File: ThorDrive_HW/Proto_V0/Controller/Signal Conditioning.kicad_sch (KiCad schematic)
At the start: 13 parts, among them U2 LM324, U3 LM324

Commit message: update
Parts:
- C3, C4, C5, C6: footprint (none) -> Capacitor_SMD:C_0805_2012Metric_Pad1.18x1.45mm_HandSolder
- R3, R4, R5: footprint (none) -> Resistor_SMD:R_1206_3216Metric_Pad1.30x1.75mm_HandSolder
- R6, R7, R8, R9: footprint (none) -> Resistor_SMD:R_0805_2012Metric_Pad1.20x1.40mm_HandSolder
- U2, U3: footprint (none) -> Package_SO:SOIC-14_3.9x8.7mm_P1.27mm
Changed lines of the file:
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@@
 			)
 		)
-		(property "Footprint" ""
+		(property "Footprint" "Package_SO:SOIC-14_3.9x8.7mm_P1.27mm"
 			(at 57.15 86.36 0)
 			(effects
@@
 			)
 		)
-		(property "Footprint" ""
+		(property "Footprint" "Resistor_SMD:R_1206_3216Metric_Pad1.30x1.75mm_HandSolder"
 			(at 47.752 127 90)
 			(effects
@@
 			)
 		)
-		(property "Footprint" ""
+		(property "Footprint" "Package_SO:SOIC-14_3.9x8.7mm_P1.27mm"
 			(at 175.26 80.01 0)
 			(effects
@@
 			)
 		)
-		(property "Footprint" ""
+		(property "Footprint" "Package_SO:SOIC-14_3.9x8.7mm_P1.27mm"
 			(at 55.88 45.72 0)
 			(effects
@@
 			)
 		)
-		(property "Footprint" ""
+		(property "Footprint" "Resistor_SMD:R_0805_2012Metric_Pad1.20x1.40mm_HandSolder"
 			(at 134.62 37.338 90)
 			(effects
@@
 			)
 		)
-		(property "Footprint" ""
+		(property "Footprint" "Resistor_SMD:R_0805_2012Metric_Pad1.20x1.40mm_HandSolder"
 			(at 137.16 124.968 90)
 			(effects
@@
 			)
 		)
-		(property "Footprint" ""
+		(property "Footprint" "Package_SO:SOIC-14_3.9x8.7mm_P1.27mm"
 			(at 176.53 123.19 0)
 			(effects
@@
 			)
 		)
-		(property "Footprint" ""
+		(property "Footprint" "Resistor_SMD:R_0805_2012Metric_Pad1.20x1.40mm_HandSolder"
 			(at 137.16 81.788 90)
 			(effects
@@
 			)
 		)
-		(property "Footprint" ""
+		(property "Footprint" "Resistor_SMD:R_1206_3216Metric_Pad1.30x1.75mm_HandSolder"
 			(at 42.672 143.51 90)
 			(effects
@@
 			)
 		)
-		(property "Footprint" ""
+		(property "Footprint" "Resistor_SMD:R_1206_3216Metric_Pad1.30x1.75mm_HandSolder"
 			(at 51.562 143.51 90)
 			(effects
@@
 			)
 		)
-		(property "Footprint" ""
+		(property "Footprint" "Package_SO:SOIC-14_3.9x8.7mm_P1.27mm"
 			(at 255.27 29.21 0)
 			(effects
@@
 			)
 		)
-		(property "Footprint" ""
+		(property "Footprint" "Package_SO:SOIC-14_3.9x8.7mm_P1.27mm"
 			(at 243.84 63.5 0)
 			(effects
@@
 			)
 		)
-		(property "Footprint" ""
+		(property "Footprint" "Capacitor_SMD:C_0805_2012Metric_Pad1.18x1.45mm_HandSolder"
 			(at 140.6652 43.18 0)
 			(effects
@@
 			)
 		)
-		(property "Footprint" ""
+		(property "Footprint" "Package_SO:SOIC-14_3.9x8.7mm_P1.27mm"
 			(at 55.88 24.13 0)
 			(effects
@@
 			)
 		)
-		(property "Footprint" ""
+		(property "Footprint" "Capacitor_SMD:C_0805_2012Metric_Pad1.18x1.45mm_HandSolder"
 			(at 82.2452 100.33 0)
 			(effects
@@
 			)
 		)
-		(property "Footprint" ""
+		(property "Footprint" "Package_SO:SOIC-14_3.9x8.7mm_P1.27mm"
 			(at 265.43 63.5 0)
 			(effects
@@
 			)
 		)
-		(property "Footprint" ""
+		(property "Footprint" "Capacitor_SMD:C_0805_2012Metric_Pad1.18x1.45mm_HandSolder"
 			(at 143.2052 88.9 0)
 			(effects
@@
 			)
 		)
-		(property "Footprint" ""
+		(property "Footprint" "Package_SO:SOIC-14_3.9x8.7mm_P1.27mm"
 			(at 57.15 64.77 0)
 			(effects
@@
 			)
 		)
-		(property "Footprint" ""
+		(property "Footprint" "Resistor_SMD:R_0805_2012Metric_Pad1.20x1.40mm_HandSolder"
 			(at 74.93 90.678 90)
 			(effects
@@
 			)
 		)
-		(property "Footprint" ""
+		(property "Footprint" "Package_SO:SOIC-14_3.9x8.7mm_P1.27mm"
 			(at 176.53 35.56 0)
 			(effects
@@
 			)
 		)
-		(property "Footprint" ""
+		(property "Footprint" "Capacitor_SMD:C_0805_2012Metric_Pad1.18x1.45mm_HandSolder"
 			(at 143.2052 133.35 0)
 			(effects

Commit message: Routing Try0
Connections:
- net CG_voltageBuff: now also U3.13 (-), U3.14; no longer U3.8, U3.9 (-)
- net PhaseC voltage: now also U3.12 (+); no longer U3.10 (+)
- net VN: now also U3.10 (+); no longer U3.12 (+)
- net emfZCD_A: now also U2.7; no longer U2.1
- net emfZCD_B: now also U2.1; no longer U2.7
- net at C5.1, R8.2: now also U2.3 (+); no longer U2.5 (+)
- net at C4.1, R7.2: now also U2.5 (+); no longer U2.3 (+)
- new net: R6.1, U3.8, U3.9 (-)

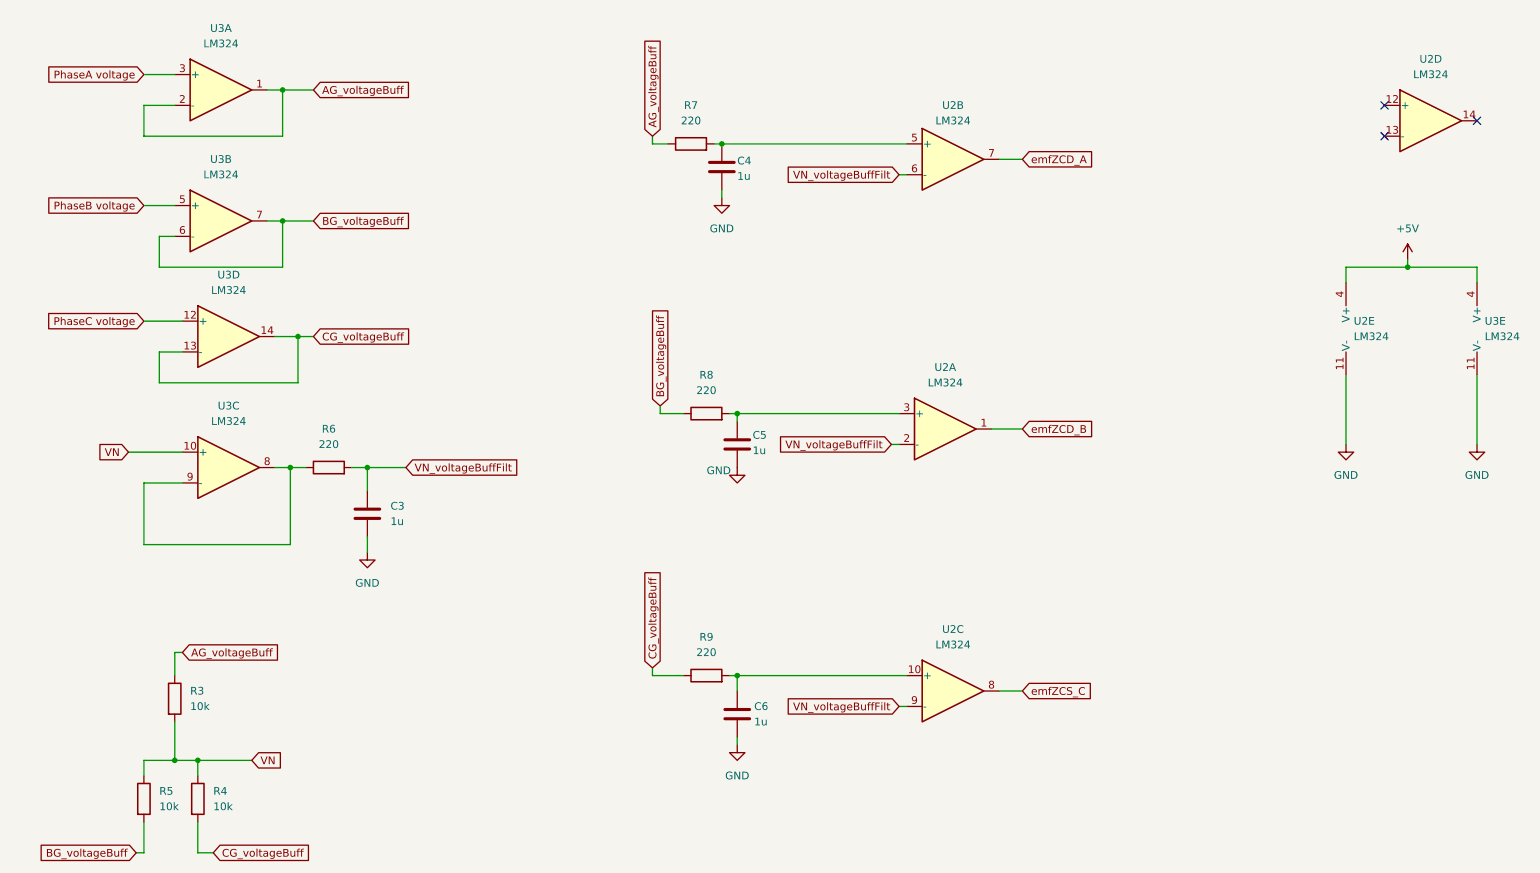
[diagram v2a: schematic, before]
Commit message: Controller Board V0 Finalized
A Controller Board simple and built upon the Atmega328p...
Single Layer Design with few jumpers.... Compatible with Inverter V0
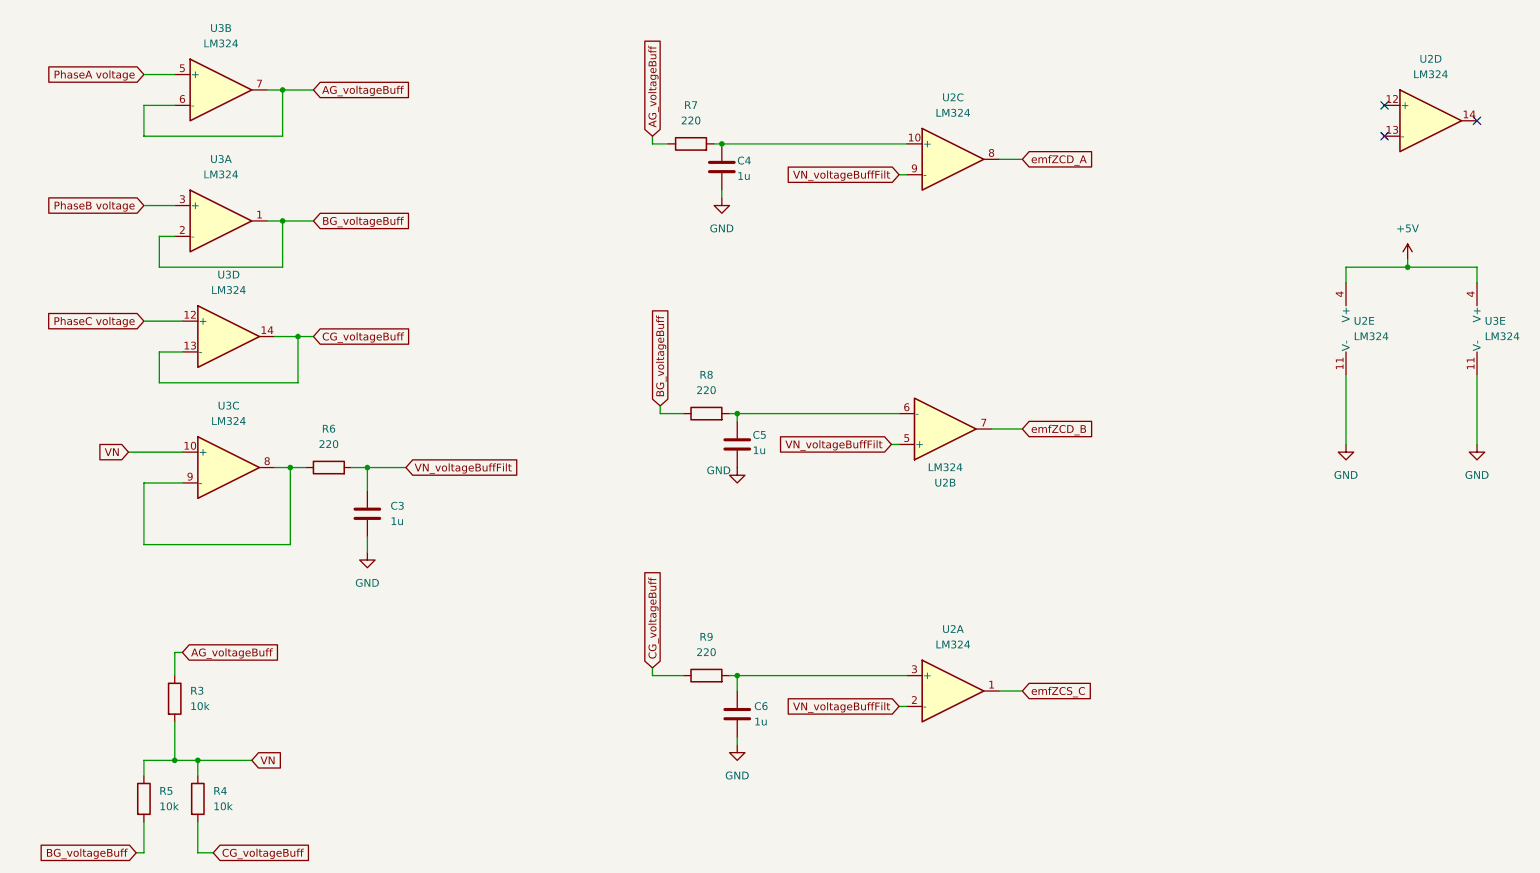
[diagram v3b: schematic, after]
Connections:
- net AG_voltageBuff: now also U3.6 (-), U3.7; no longer U3.1, U3.2 (-)
- net BG_voltageBuff: now also U3.1, U3.2 (-); no longer U3.6 (-), U3.7
- net PhaseA voltage: now also U3.5 (+); no longer U3.3 (+)
- net PhaseB voltage: now also U3.3 (+); no longer U3.5 (+)
- net VN_voltageBuffFilt: now also U2.5 (+); no longer U2.6 (-)
- net emfZCD_A: now also U2.8; no longer U2.7
- net emfZCD_B: now also U2.7; no longer U2.1
- net emfZCS_C: now also U2.1; no longer U2.8
- net at C4.1, R7.2: now also U2.10 (+); no longer U2.5 (+)
- net at C6.1, R9.2: now also U2.3 (+); no longer U2.10 (+)
- net at C5.1, R8.2: now also U2.6 (-); no longer U2.3 (+)
